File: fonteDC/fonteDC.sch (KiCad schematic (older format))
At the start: 18 parts, among them J1 Conn_01x02, T1 Transformer_1P_SS, U1 LM7805_TO220

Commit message: Tudo antes dos footprints dos capacitores e transformador
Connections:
- net GND: now reaches T1.5 (SB), switch1.4 (GND220), switch1.6 (GND110)
- net GND: now also Cc1.1, Cc1.2, Cc2.2, Ce1.1, Ce1.2, Ce2.2, D1.1 (K), D2.2 (A), D3.1 (K), D4.2 (A), D6.1 (K), F1.2, J1.2 (Pin_2), U1.1 (VI), U1.2 (GND), switch1.2 (GND)
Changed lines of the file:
@@
 	2250 2900 2250 3150
 Wire Wire Line
-	3400 3650 4000 3650
-Wire Wire Line
 	4000 3650 4000 3550
 Wire Wire Line
@@
 	3450 3350 4000 3350
 Wire Wire Line
-	3400 3250 3550 3250
-Wire Wire Line
-	3550 3250 3550 3650
-Connection ~ 3550 3650
+	3400 3250 3850 3250
 Wire Wire Line
 	3400 3100 3450 3100
@@
 	10200 3950 10200 3400
 Connection ~ 9700 3950
+$Comp
+L GND #PWR01
+U 1 1 5B24D3C0
+P 8000 4050
+F 0 "#PWR01" H 8000 3800 50  0001 C CNN
+F 1 "GND" H 8000 3900 50  0000 C CNN
+F 2 "" H 8000 4050 50  0001 C CNN
+F 3 "" H 8000 4050 50  0001 C CNN
+	1    8000 4050
+	1    0    0    -1
+$EndComp
+$Comp
+L GND #PWR02
+U 1 1 5B24D8AE
+P 1800 4350
+F 0 "#PWR02" H 1800 4100 50  0001 C CNN
+F 1 "GND" H 1800 4200 50  0000 C CNN
+F 2 "" H 1800 4350 50  0001 C CNN
+F 3 "" H 1800 4350 50  0001 C CNN
+	1    1800 4350
+	1    0    0    -1
+$EndComp
+Wire Wire Line
+	1800 4200 1800 4350
+Connection ~ 1800 4200
+Wire Wire Line
+	8000 4050 8000 3950
+Connection ~ 8000 3950
+$Comp
+L GND #PWR03
+U 1 1 5B250636
+P 3750 3700
+F 0 "#PWR03" H 3750 3450 50  0001 C CNN
+F 1 "GND" H 3750 3550 50  0000 C CNN
+F 2 "" H 3750 3700 50  0001 C CNN
+F 3 "" H 3750 3700 50  0001 C CNN
+	1    3750 3700
+	1    0    0    -1
+$EndComp
+Wire Wire Line
+	3400 3650 4000 3650
+Wire Wire Line
+	3850 3250 3850 3550
+Wire Wire Line
+	3850 3550 4000 3550
+Wire Wire Line
+	3750 3700 3750 3650
+Connection ~ 3750 3650
 $EndSCHEMATC

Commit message: Adicionando capacitores e porta fusível
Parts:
- AC_in1: footprint (none) -> fonteDC:AC_in
- Cc1, Cc2: footprint (none) -> fonteDC:C_Disc_D5.0mm_W2.5mm_P5.00mm
- D1, D2, D3, D4: footprint (none) -> fonteDC:D_5W_P12.70mm_Horizontal
- D5, D6: footprint (none) -> fonteDC:LED_D8.0mm
- F1: footprint (none) -> fonteDC:Fuseholder5x20_horiz_SemiClosed_Casing10x25mm
- R1, R2: footprint (none) -> fonteDC:R_Axial_DIN0204_L3.6mm_D1.6mm_P7.62mm_Horizontal
- U1: footprint TO_SOT_Packages_THT:TO-220_Vertical -> fonteDC:TO-220-3_Vertical
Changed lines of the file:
@@
 F 0 "AC_in1" H 900 3250 60  0000 C CNN
 F 1 "AC_in" H 900 3350 60  0000 C CNN
-F 2 "" H 900 3250 60  0001 C CNN
+F 2 "fonteDC:AC_in" H 900 3250 60  0001 C CNN
 F 3 "" H 900 3250 60  0001 C CNN
 	1    1250 3250
@@
 F 0 "F1" V 1330 3900 50  0000 C CNN
 F 1 "Fuse" V 1175 3900 50  0000 C CNN
-F 2 "" V 1180 3900 50  0001 C CNN
+F 2 "fonteDC:Fuseholder5x20_horiz_SemiClosed_Casing10x25mm" V 1180 3900 50  0001 C CNN
 F 3 "" H 1250 3900 50  0001 C CNN
 	1    1250 3900
@@
 F 0 "R1" V 5480 3100 50  0000 C CNN
 F 1 "R" V 5400 3100 50  0000 C CNN
-F 2 "" V 5330 3100 50  0001 C CNN
+F 2 "fonteDC:R_Axial_DIN0204_L3.6mm_D1.6mm_P7.62mm_Horizontal" V 5330 3100 50  0001 C CNN
 F 3 "" H 5400 3100 50  0001 C CNN
 	1    5400 3100
@@
 F 0 "D5" H 5400 3650 50  0000 C CNN
 F 1 "LED" H 5400 3450 50  0000 C CNN
-F 2 "" H 5400 3550 50  0001 C CNN
+F 2 "fonteDC:LED_D8.0mm" H 5400 3550 50  0001 C CNN
 F 3 "" H 5400 3550 50  0001 C CNN
 	1    5400 3550
@@
 F 0 "D1" H 6100 2850 50  0000 C CNN
 F 1 "D" H 6100 2650 50  0000 C CNN
-F 2 "" H 6100 2750 50  0001 C CNN
+F 2 "fonteDC:D_5W_P12.70mm_Horizontal" H 6100 2750 50  0001 C CNN
 F 3 "" H 6100 2750 50  0001 C CNN
 	1    6100 2750
@@
 F 0 "D2" H 6100 4050 50  0000 C CNN
 F 1 "D" H 6100 3850 50  0000 C CNN
-F 2 "" H 6100 3950 50  0001 C CNN
+F 2 "fonteDC:D_5W_P12.70mm_Horizontal" H 6100 3950 50  0001 C CNN
 F 3 "" H 6100 3950 50  0001 C CNN
 	1    6100 3950
@@
 F 0 "D3" H 6450 3250 50  0000 C CNN
 F 1 "D" H 6450 3050 50  0000 C CNN
-F 2 "" H 6450 3150 50  0001 C CNN
+F 2 "fonteDC:D_5W_P12.70mm_Horizontal" H 6450 3150 50  0001 C CNN
 F 3 "" H 6450 3150 50  0001 C CNN
 	1    6450 3150
@@
 F 0 "D4" H 6450 3700 50  0000 C CNN
 F 1 "D" H 6450 3500 50  0000 C CNN
-F 2 "" H 6450 3600 50  0001 C CNN
+F 2 "fonteDC:D_5W_P12.70mm_Horizontal" H 6450 3600 50  0001 C CNN
 F 3 "" H 6450 3600 50  0001 C CNN
 	1    6450 3600
@@
 F 0 "Cc1" H 7675 3500 50  0000 L CNN
 F 1 "C" H 7675 3300 50  0000 L CNN
-F 2 "" H 7688 3250 50  0001 C CNN
+F 2 "fonteDC:C_Disc_D5.0mm_W2.5mm_P5.00mm" H 7688 3250 50  0001 C CNN
 F 3 "" H 7650 3400 50  0001 C CNN
 	1    7650 3400
@@
 F 0 "U1" H 8150 2875 50  0000 C CNN
 F 1 "LM7805_TO220" H 8300 2875 50  0000 L CNN
-F 2 "TO_SOT_Packages_THT:TO-220_Vertical" H 8300 2975 50  0001 C CIN
+F 2 "fonteDC:TO-220-3_Vertical" H 8300 2975 50  0001 C CIN
 F 3 "" H 8300 2700 50  0001 C CNN
 	1    8300 2750
@@
 F 0 "Cc2" H 9275 3500 50  0000 L CNN
 F 1 "C" H 9275 3300 50  0000 L CNN
-F 2 "" H 9288 3250 50  0001 C CNN
+F 2 "fonteDC:C_Disc_D5.0mm_W2.5mm_P5.00mm" H 9288 3250 50  0001 C CNN
 F 3 "" H 9250 3400 50  0001 C CNN
 	1    9250 3400
@@
 F 0 "R2" V 9780 3050 50  0000 C CNN
 F 1 "R" V 9700 3050 50  0000 C CNN
-F 2 "" V 9630 3050 50  0001 C CNN
+F 2 "fonteDC:R_Axial_DIN0204_L3.6mm_D1.6mm_P7.62mm_Horizontal" V 9630 3050 50  0001 C CNN
 F 3 "" H 9700 3050 50  0001 C CNN
 	1    9700 3050
@@
 F 0 "D6" H 9700 3600 50  0000 C CNN
 F 1 "LED" H 9700 3400 50  0000 C CNN
-F 2 "" H 9700 3500 50  0001 C CNN
+F 2 "fonteDC:LED_D8.0mm" H 9700 3500 50  0001 C CNN
 F 3 "" H 9700 3500 50  0001 C CNN
 	1    9700 3500

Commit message: Adicionando footprints da chave seletora de tensão e do transformador
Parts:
- Ce1: footprint (none) -> fonteDC:CP_elet_7mF
- Ce2: footprint (none) -> fonteDC:CP_elet_10mF
- F1: footprint fonteDC:Fuseholder5x20_horiz_SemiClosed_Casing10x25mm -> fonteDC:fuseholder
- T1: footprint (none) -> fonteDC:transformer
- switch1: footprint (none) -> fonteDC:swich_110_220
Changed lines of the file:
@@
 F 0 "T1" H 4400 3600 50  0000 C CNN
 F 1 "Transformer_1P_SS" H 4400 3050 50  0000 C CNN
-F 2 "" H 4400 3350 50  0001 C CNN
+F 2 "fonteDC:transformer" H 4400 3350 50  0001 C CNN
 F 3 "" H 4400 3350 50  0001 C CNN
 	1    4400 3350
@@
 F 0 "switch1" H 2800 3000 60  0000 C CNN
 F 1 "voltage_switch" H 2800 3950 60  0000 C CNN
-F 2 "" H 2800 3000 60  0001 C CNN
+F 2 "fonteDC:swich_110_220" H 2800 3000 60  0001 C CNN
 F 3 "" H 2800 3000 60  0001 C CNN
 	1    2650 3400
@@
 F 0 "F1" V 1330 3900 50  0000 C CNN
 F 1 "Fuse" V 1175 3900 50  0000 C CNN
-F 2 "fonteDC:Fuseholder5x20_horiz_SemiClosed_Casing10x25mm" V 1180 3900 50  0001 C CNN
+F 2 "fonteDC:fuseholder" V 1180 3900 50  0001 C CNN
 F 3 "" H 1250 3900 50  0001 C CNN
 	1    1250 3900
@@
 F 0 "Ce1" H 7375 3500 50  0000 L CNN
 F 1 "CP1" H 7375 3300 50  0000 L CNN
-F 2 "" H 7350 3400 50  0001 C CNN
+F 2 "fonteDC:CP_elet_7mF" H 7350 3400 50  0001 C CNN
 F 3 "" H 7350 3400 50  0001 C CNN
 	1    7350 3400
@@
 F 0 "Ce2" H 8925 3500 50  0000 L CNN
 F 1 "CP1" H 8925 3300 50  0000 L CNN
-F 2 "" H 8900 3400 50  0001 C CNN
+F 2 "fonteDC:CP_elet_10mF" H 8900 3400 50  0001 C CNN
 F 3 "" H 8900 3400 50  0001 C CNN
 	1    8900 3400

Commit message: almost done.
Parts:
- D5, D6: footprint fonteDC:LED_D8.0mm -> Diodes_THT:D_T-1_P12.70mm_Horizontal
- J1: footprint (none) -> fonteDC:AC_in
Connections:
- removed net GND: Cc1.1, Cc1.2, Cc2.2, Ce1.1, Ce1.2, Ce2.2, D1.1 (K), D2.2 (A), D3.1 (K), D4.2 (A), D6.1 (K), F1.2, J1.2 (Pin_2), T1.5 (SB), U1.1 (VI), U1.2 (GND), switch1.2 (GND), switch1.4 (GND220), switch1.6 (GND110)
- new net: T1.5 (SB), switch1.4 (GND220), switch1.6 (GND110)
- new net: F1.2, switch1.2 (GND)
- new net: Cc1.1, Ce1.1, D1.1 (K), D3.1 (K), U1.1 (VI)
- new net: Cc1.2, Cc2.2, Ce1.2, Ce2.2, D2.2 (A), D4.2 (A), D6.1 (K), J1.2 (Pin_2), U1.2 (GND)
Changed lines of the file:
@@
 F 0 "D5" H 5400 3650 50  0000 C CNN
 F 1 "LED" H 5400 3450 50  0000 C CNN
-F 2 "fonteDC:LED_D8.0mm" H 5400 3550 50  0001 C CNN
+F 2 "Diodes_THT:D_T-1_P12.70mm_Horizontal" H 5400 3550 50  0001 C CNN
 F 3 "" H 5400 3550 50  0001 C CNN
 	1    5400 3550
@@
 $EndComp
 Wire Wire Line
-	5750 2750 5750 3600
-Wire Wire Line
-	5750 3600 6300 3600
-Connection ~ 5750 2750
-Wire Wire Line
-	5850 3950 5850 3150
-Wire Wire Line
 	5850 3150 6300 3150
 Connection ~ 5850 3950
@@
 	6250 3950 10200 3950
 Wire Wire Line
-	6900 3950 6900 2750
-Wire Wire Line
 	6250 2750 8000 2750
 Wire Wire Line
-	6600 3150 6900 3150
-Connection ~ 6900 3150
-Wire Wire Line
-	6600 3600 6900 3600
-Connection ~ 6900 3600
+	6600 3150 7350 3150
+Wire Wire Line
+	6600 3600 7350 3600
 $Comp
 L CP1 Ce1
@@
 Wire Wire Line
 	7350 2750 7350 3250
-Connection ~ 6900 2750
 Wire Wire Line
 	7350 3950 7350 3550
-Connection ~ 6900 3950
 Wire Wire Line
 	7350 3050 7650 3050
@@
 F 0 "D6" H 9700 3600 50  0000 C CNN
 F 1 "LED" H 9700 3400 50  0000 C CNN
-F 2 "fonteDC:LED_D8.0mm" H 9700 3500 50  0001 C CNN
+F 2 "Diodes_THT:D_T-1_P12.70mm_Horizontal" H 9700 3500 50  0001 C CNN
 F 3 "" H 9700 3500 50  0001 C CNN
 	1    9700 3500
@@
 F 0 "J1" H 10400 3400 50  0000 C CNN
 F 1 "Conn_01x02" H 10400 3100 50  0000 C CNN
-F 2 "" H 10400 3300 50  0001 C CNN
+F 2 "fonteDC:AC_in" H 10400 3300 50  0001 C CNN
 F 3 "" H 10400 3300 50  0001 C CNN
 	1    10400 3300
@@
 	10200 3950 10200 3400
 Connection ~ 9700 3950
-$Comp
-L GND #PWR01
-U 1 1 5B24D3C0
-P 8000 4050
-F 0 "#PWR01" H 8000 3800 50  0001 C CNN
-F 1 "GND" H 8000 3900 50  0000 C CNN
-F 2 "" H 8000 4050 50  0001 C CNN
-F 3 "" H 8000 4050 50  0001 C CNN
-	1    8000 4050
-	1    0    0    -1
-$EndComp
-$Comp
-L GND #PWR02
-U 1 1 5B24D8AE
-P 1800 4350
-F 0 "#PWR02" H 1800 4100 50  0001 C CNN
-F 1 "GND" H 1800 4200 50  0000 C CNN
-F 2 "" H 1800 4350 50  0001 C CNN
-F 3 "" H 1800 4350 50  0001 C CNN
-	1    1800 4350
-	1    0    0    -1
-$EndComp
-Wire Wire Line
-	1800 4200 1800 4350
-Connection ~ 1800 4200
-Wire Wire Line
-	8000 4050 8000 3950
-Connection ~ 8000 3950
-$Comp
-L GND #PWR03
-U 1 1 5B250636
-P 3750 3700
-F 0 "#PWR03" H 3750 3450 50  0001 C CNN
-F 1 "GND" H 3750 3550 50  0000 C CNN
-F 2 "" H 3750 3700 50  0001 C CNN
-F 3 "" H 3750 3700 50  0001 C CNN
-	1    3750 3700
-	1    0    0    -1
-$EndComp
 Wire Wire Line
 	3400 3650 4000 3650
@@
 	3850 3550 4000 3550
 Wire Wire Line
-	3750 3700 3750 3650
-Connection ~ 3750 3650
+	5850 3950 5850 3150
+Connection ~ 7350 3150
+Connection ~ 7350 3600
+Wire Wire Line
+	6300 3600 5900 3600
+Wire Wire Line
+	5900 3600 5900 2750
+Connection ~ 5900 2750
 $EndSCHEMATC

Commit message: Finished.
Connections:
- net at AC_in1.1 (V+), switch1.1 (VDD): now also R1.1
- net at D2.1 (K), D3.2 (A), T1.1 (AA): no longer D5.1 (K)
- net at D1.2 (A), D4.1 (K), T1.2 (AB): no longer R1.1
- net at F1.2, switch1.2 (GND): now also D5.1 (K)
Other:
- moved on the sheet: D5, R1
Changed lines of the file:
@@
 	1    0    0    -1
 $EndComp
-Wire Wire Line
-	1250 3600 1250 3750
-Wire Wire Line
-	1250 4050 1250 4200
-Wire Wire Line
-	1250 4200 2250 4200
-Wire Wire Line
-	2250 4200 2250 3600
-Wire Wire Line
-	1250 2900 2250 2900
-Wire Wire Line
-	2250 2900 2250 3150
-Wire Wire Line
-	4000 3650 4000 3550
-Wire Wire Line
-	3400 3500 3450 3500
-Wire Wire Line
-	3450 3500 3450 3350
-Wire Wire Line
-	3450 3350 4000 3350
-Wire Wire Line
-	3400 3250 3850 3250
-Wire Wire Line
-	3400 3100 3450 3100
-Wire Wire Line
-	3450 3100 3450 3150
-Wire Wire Line
-	3450 3150 4000 3150
 $Comp
 L R R1
 U 1 1 5B241B31
-P 5400 3100
-F 0 "R1" V 5480 3100 50  0000 C CNN
-F 1 "R" V 5400 3100 50  0000 C CNN
-F 2 "fonteDC:R_Axial_DIN0204_L3.6mm_D1.6mm_P7.62mm_Horizontal" V 5330 3100 50  0001 C CNN
-F 3 "" H 5400 3100 50  0001 C CNN
-	1    5400 3100
+P 1850 3150
+F 0 "R1" V 1930 3150 50  0000 C CNN
+F 1 "R" V 1850 3150 50  0000 C CNN
+F 2 "fonteDC:R_Axial_DIN0204_L3.6mm_D1.6mm_P7.62mm_Horizontal" V 1780 3150 50  0001 C CNN
+F 3 "" H 1850 3150 50  0001 C CNN
+	1    1850 3150
 	1    0    0    -1
 $EndComp
@@
 L LED D5
 U 1 1 5B241BF9
-P 5400 3550
-F 0 "D5" H 5400 3650 50  0000 C CNN
-F 1 "LED" H 5400 3450 50  0000 C CNN
-F 2 "Diodes_THT:D_T-1_P12.70mm_Horizontal" H 5400 3550 50  0001 C CNN
-F 3 "" H 5400 3550 50  0001 C CNN
-	1    5400 3550
+P 1850 3500
+F 0 "D5" H 1850 3600 50  0000 C CNN
+F 1 "LED" H 1850 3400 50  0000 C CNN
+F 2 "Diodes_THT:D_T-1_P12.70mm_Horizontal" H 1850 3500 50  0001 C CNN
+F 3 "" H 1850 3500 50  0001 C CNN
+	1    1850 3500
 	0    -1   -1   0
 $EndComp
-Wire Wire Line
-	4800 3150 4800 2750
-Wire Wire Line
-	4800 2750 5950 2750
-Wire Wire Line
-	5400 2750 5400 2950
-Wire Wire Line
-	4800 3550 4800 3950
-Wire Wire Line
-	4800 3950 5950 3950
-Wire Wire Line
-	5400 3950 5400 3700
-Wire Wire Line
-	5400 3250 5400 3400
 $Comp
 L D D1
@@
 	1    0    0    -1
 $EndComp
-Connection ~ 5400 2750
-Connection ~ 5400 3950
 $Comp
 L D D3
@@
 	1    0    0    -1
 $EndComp
-Wire Wire Line
-	5850 3150 6300 3150
-Connection ~ 5850 3950
-Wire Wire Line
-	6250 3950 10200 3950
-Wire Wire Line
-	6250 2750 8000 2750
-Wire Wire Line
-	6600 3150 7350 3150
-Wire Wire Line
-	6600 3600 7350 3600
 $Comp
 L CP1 Ce1
@@
 	1    0    0    -1
 $EndComp
-Wire Wire Line
-	7350 2750 7350 3250
-Wire Wire Line
-	7350 3950 7350 3550
-Wire Wire Line
-	7350 3050 7650 3050
-Wire Wire Line
-	7650 3050 7650 3250
-Connection ~ 7350 3050
-Wire Wire Line
-	7650 3550 7650 3750
-Wire Wire Line
-	7650 3750 7350 3750
-Connection ~ 7350 3750
-Connection ~ 7350 2750
-Wire Wire Line
-	8300 3950 8300 3050
-Connection ~ 7350 3950
 $Comp
 L CP1 Ce2
@@
 	1    0    0    -1
 $EndComp
-Wire Wire Line
-	8600 2750 10200 2750
-Wire Wire Line
-	8900 2750 8900 3250
-Wire Wire Line
-	8900 3050 9250 3050
-Wire Wire Line
-	9250 3050 9250 3250
-Connection ~ 8900 3050
-Wire Wire Line
-	8900 3950 8900 3550
-Connection ~ 8300 3950
-Wire Wire Line
-	8900 3750 9250 3750
-Wire Wire Line
-	9250 3750 9250 3550
-Connection ~ 8900 3750
 $Comp
 L R R2
@@
 	0    -1   -1   0
 $EndComp
-Wire Wire Line
-	9700 2750 9700 2900
-Connection ~ 8900 2750
-Wire Wire Line
-	9700 3200 9700 3350
-Wire Wire Line
-	9700 3950 9700 3650
-Connection ~ 8900 3950
 $Comp
 L Conn_01x02 J1
@@
 $EndComp
 Wire Wire Line
+	1250 3600 1250 3750
+Wire Wire Line
+	1250 4050 1250 4200
+Wire Wire Line
+	1250 4200 2250 4200
+Wire Wire Line
+	2250 4200 2250 3600
+Wire Wire Line
+	1250 2900 2250 2900
+Wire Wire Line
+	2250 2900 2250 3150
+Wire Wire Line
+	4000 3650 4000 3550
+Wire Wire Line
+	3400 3500 3450 3500
+Wire Wire Line
+	3450 3500 3450 3350
+Wire Wire Line
+	3450 3350 4000 3350
+Wire Wire Line
+	3400 3250 3850 3250
+Wire Wire Line
+	3400 3100 3450 3100
+Wire Wire Line
+	3450 3100 3450 3150
+Wire Wire Line
+	3450 3150 4000 3150
+Wire Wire Line
+	4800 3150 4800 2750
+Wire Wire Line
+	4800 2750 5950 2750
+Wire Wire Line
+	4800 3550 4800 3950
+Wire Wire Line
+	4800 3950 5950 3950
+Wire Wire Line
+	1850 3650 1850 4200
+Wire Wire Line
+	5850 3150 6300 3150
+Connection ~ 5850 3950
+Wire Wire Line
+	6250 3950 10200 3950
+Wire Wire Line
+	6250 2750 8000 2750
+Wire Wire Line
+	6600 3150 7350 3150
+Wire Wire Line
+	6600 3600 7350 3600
+Wire Wire Line
+	7350 2750 7350 3250
+Wire Wire Line
+	7350 3950 7350 3550
+Wire Wire Line
+	7350 3050 7650 3050
+Wire Wire Line
+	7650 3050 7650 3250
+Connection ~ 7350 3050
+Wire Wire Line
+	7650 3550 7650 3750
+Wire Wire Line
+	7650 3750 7350 3750
+Connection ~ 7350 3750
+Connection ~ 7350 2750
+Wire Wire Line
+	8300 3950 8300 3050
+Connection ~ 7350 3950
+Wire Wire Line
+	8600 2750 10200 2750
+Wire Wire Line
+	8900 2750 8900 3250
+Wire Wire Line
+	8900 3050 9250 3050
+Wire Wire Line
+	9250 3050 9250 3250
+Connection ~ 8900 3050
+Wire Wire Line
+	8900 3950 8900 3550
+Connection ~ 8300 3950
+Wire Wire Line
+	8900 3750 9250 3750
+Wire Wire Line
+	9250 3750 9250 3550
+Connection ~ 8900 3750
+Wire Wire Line
+	9700 2750 9700 2900
+Connection ~ 8900 2750
+Wire Wire Line
+	9700 3200 9700 3350
+Wire Wire Line
+	9700 3950 9700 3650
+Connection ~ 8900 3950
+Wire Wire Line
 	10200 2750 10200 3300
 Connection ~ 9700 2750
@@
 	5900 3600 5900 2750
 Connection ~ 5900 2750
+Wire Wire Line
+	1850 3350 1850 3300
+Wire Wire Line
+	1850 3000 1850 2900
+Connection ~ 1850 2900
+Connection ~ 1850 4200
 $EndSCHEMATC

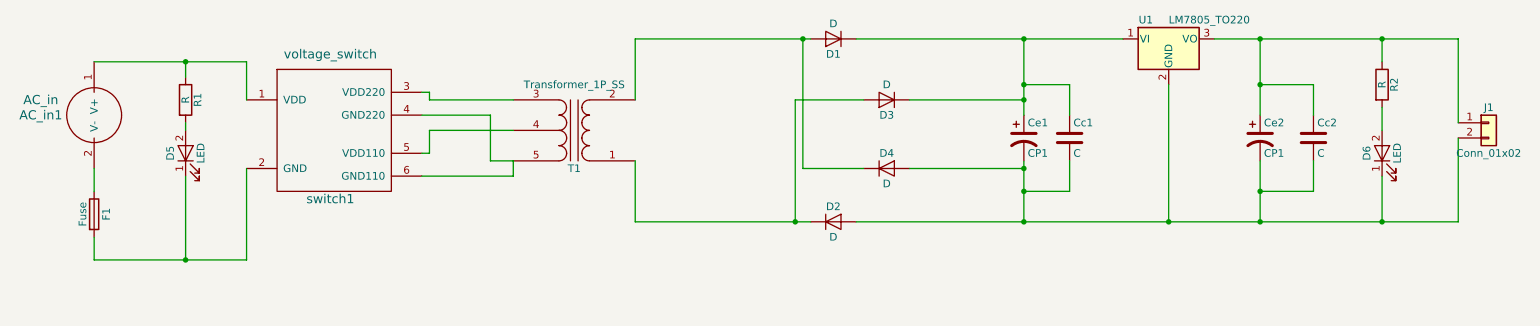
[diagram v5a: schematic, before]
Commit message: Organizando o esquemático final
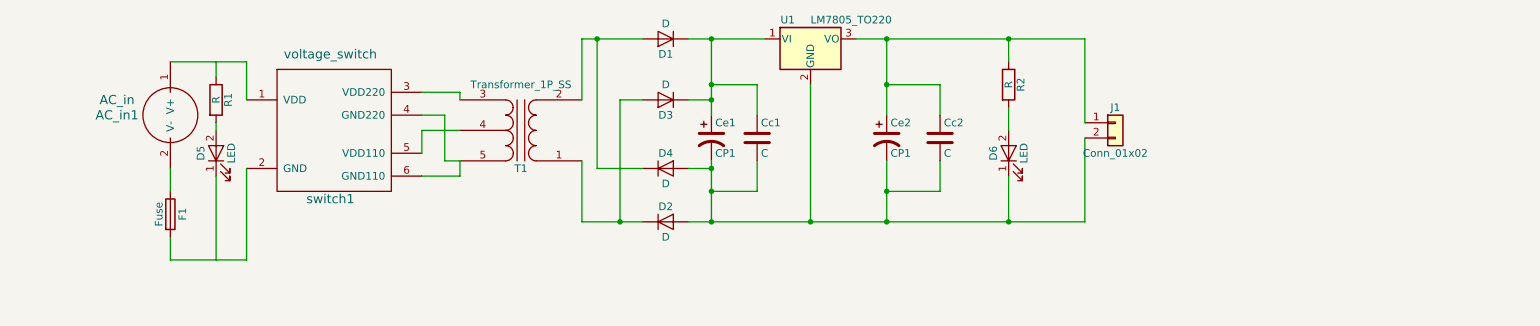
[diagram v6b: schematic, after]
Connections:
- wire segments 51 -> 49
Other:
- moved on the sheet: AC_in1, Cc1, Cc2, Ce1, Ce2, D1, D2, D3, D4, D5, D6, F1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
